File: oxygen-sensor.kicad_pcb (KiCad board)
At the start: 2 copper layers, 37.5 x 137.5 mm, 38 parts, among them J1 DEBUG, J2 UART, J3 I2C, U1 LM358, U2 LD1117S33TR_SOT223, U3 STM32F030K6Tx, Y1 Crystal

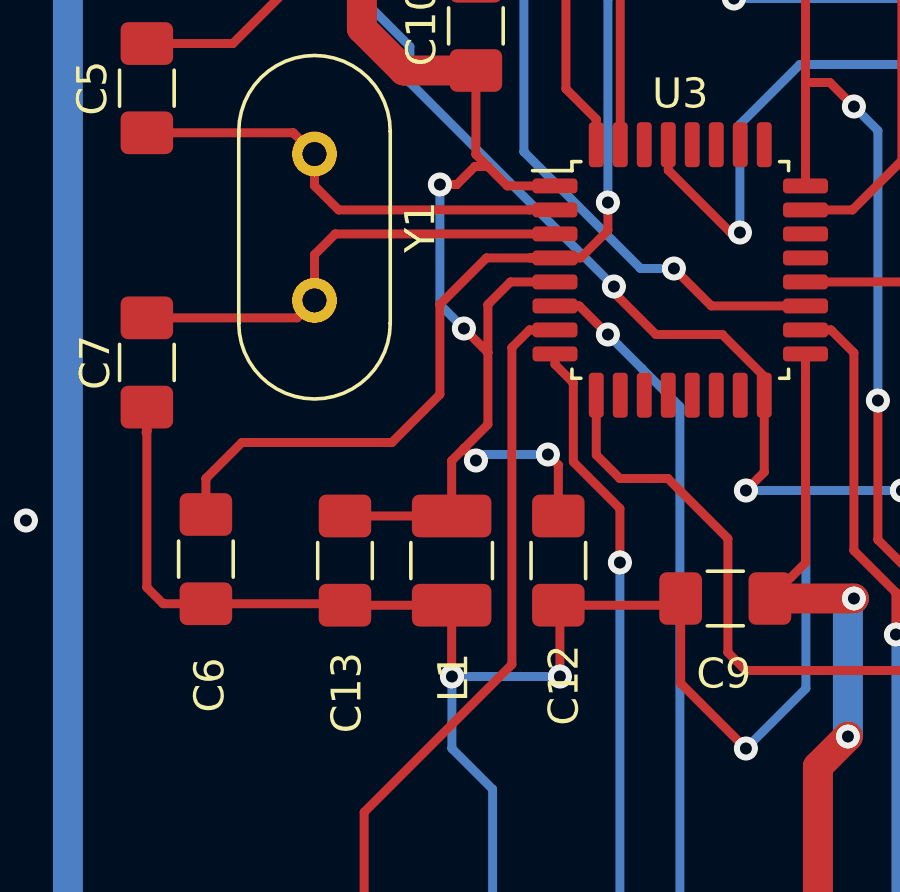
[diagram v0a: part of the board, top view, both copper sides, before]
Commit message: Fix short-circuit error
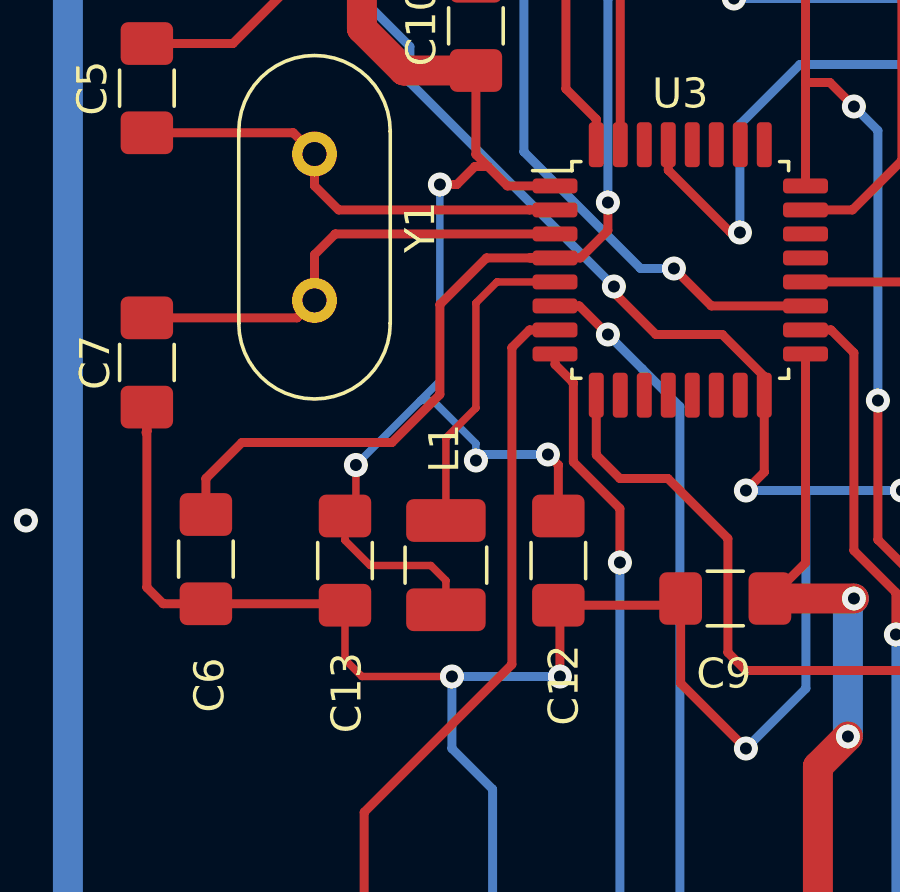
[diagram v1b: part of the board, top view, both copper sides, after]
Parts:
- moved L1 0.24 mm to (63.0, 74.5), turned to 270 degrees
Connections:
- L1 pad 1: GND -> Net-(L1-Pad1)
- U3 pad 5: +3V3 -> Net-(L1-Pad1)
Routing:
- net Net-(L1-Pad1): track 0.00 -> 10.6 mm
- net +3V3: track 302.4 -> 303.0 mm
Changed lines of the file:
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@@
     (thickness 1.6)
     (drawings 24)
-    (tracks 446)
+    (tracks 453)
     (zones 0)
     (modules 38)
-    (nets 37)
+    (nets 38)
   )
   (page A4)
@@
   (net 35 "Net-(U3-Pad28)")
   (net 36 "Net-(U3-Pad30)")
+  (net 37 "Net-(L1-Pad1)")
   (net_class Default "This is the default net class."
     (clearance 0.2)
@@
     (add_net "Net-(J3-Pad2)")
     (add_net "Net-(J3-Pad3)")
+    (add_net "Net-(L1-Pad1)")
     (add_net "Net-(R1-Pad1)")
     (add_net "Net-(R10-Pad1)")
@@
   )
   (module Inductor_SMD:L_1210_3225Metric_Pad1.42x2.65mm_HandSolder (layer F.Cu)
-    (at 63.192 74.3365 90)
+    (at 63 74.4875 270)
     (descr "Capacitor SMD 1210 (3225 Metric), square (rectangular) end terminal, IPC_7351 nominal with elongated pad for handsoldering. (Body size source: http://www.tortai-tech.com/upload/download/2011102023233369053.pdf), generated with kicad-footprint-generator")
     (tags "inductor handsolder")
     (attr smd)
-    (fp_text reference L1 (at -3.8955 0.054 90) (layer F.SilkS)
-      (effects (font (size 1 1) (thickness 0.15)))
-    )
-    (fp_text value 22uH (at 0 2.28 90) (layer F.Fab)
+    (fp_text reference L1 (at -3.8955 0.054 270) (layer F.SilkS)
+      (effects (font (size 1 1) (thickness 0.15)))
+    )
+    (fp_text value 22uH (at 0 2.28 270) (layer F.Fab)
       (effects (font (size 1 1) (thickness 0.15)))
     )
@@
     (fp_line (start 2.45 -1.58) (end 2.45 1.58) (layer F.CrtYd) (width 0.05))
     (fp_line (start 2.45 1.58) (end -2.45 1.58) (layer F.CrtYd) (width 0.05))
-    (fp_text user %R (at 0 0 90) (layer F.Fab)
+    (fp_text user %R (at 0 0 270) (layer F.Fab)
       (effects (font (size 0.8 0.8) (thickness 0.12)))
     )
-    (pad 1 smd roundrect (at -1.4875 0 90) (size 1.425 2.65) (layers F.Cu F.Paste F.Mask) (roundrect_rratio 0.175439)
-      (net 1 GND))
-    (pad 2 smd roundrect (at 1.4875 0 90) (size 1.425 2.65) (layers F.Cu F.Paste F.Mask) (roundrect_rratio 0.175439)
+    (pad 1 smd roundrect (at -1.4875 0 270) (size 1.425 2.65) (layers F.Cu F.Paste F.Mask) (roundrect_rratio 0.175439)
+      (net 37 "Net-(L1-Pad1)"))
+    (pad 2 smd roundrect (at 1.4875 0 270) (size 1.425 2.65) (layers F.Cu F.Paste F.Mask) (roundrect_rratio 0.175439)
       (net 8 +3V3))
     (model ${KISYS3DMOD}/Inductor_SMD.3dshapes/L_1210_3225Metric.wrl
@@
       (net 14 /NRST))
     (pad 5 smd roundrect (at -4.175 0.4) (size 1.5 0.5) (layers F.Cu F.Paste F.Mask) (roundrect_rratio 0.25)
-      (net 8 +3V3))
+      (net 37 "Net-(L1-Pad1)"))
     (pad 6 smd roundrect (at -4.175 1.2) (size 1.5 0.5) (layers F.Cu F.Paste F.Mask) (roundrect_rratio 0.25)
       (net 9 /OUT1))
@@
   (segment (start 59.587 75.775) (end 59.636 75.824) (width 0.3) (layer F.Cu) (net 1))
   (segment (start 55 75.775) (end 59.587 75.775) (width 0.3) (layer F.Cu) (net 1))
-  (segment (start 59.636 75.824) (end 63.192 75.824) (width 0.3) (layer F.Cu) (net 1))
   (segment (start 70.601 75.824) (end 70.825 75.6) (width 0.3) (layer F.Cu) (net 1))
   (segment (start 66.748 75.824) (end 70.601 75.824) (width 0.3) (layer F.Cu) (net 1))
-  (segment (start 63.192 75.824) (end 63.192 78.192) (width 0.3) (layer F.Cu) (net 1))
   (via (at 63.2 78.2) (size 0.8) (drill 0.4) (layers F.Cu B.Cu) (net 1))
   (segment (start 63.192 78.192) (end 63.2 78.2) (width 0.3) (layer F.Cu) (net 1))
@@
   (via (at 83 57) (size 0.8) (drill 0.4) (layers F.Cu B.Cu) (net 1))
   (via (at 63 86) (size 0.8) (drill 0.4) (layers F.Cu B.Cu) (net 1))
+  (segment (start 59.636 75.824) (end 59.636 77.636) (width 0.25) (layer F.Cu) (net 1))
+  (segment (start 60.2 78.2) (end 63.2 78.2) (width 0.25) (layer F.Cu) (net 1))
+  (segment (start 59.636 77.636) (end 60.2 78.2) (width 0.25) (layer F.Cu) (net 1))
   (segment (start 57.6 151.6) (end 62.4 151.6) (width 0.3) (layer F.Cu) (net 2))
   (segment (start 57.175 124.2) (end 57.2 124.225) (width 0.3) (layer F.Cu) (net 3))
@@
   (segment (start 78.375 135.425) (end 72.4 135.425) (width 0.3) (layer F.Cu) (net 7))
   (segment (start 81.4 132.4) (end 78.375 135.425) (width 0.3) (layer F.Cu) (net 7))
-  (segment (start 66.637 65.048) (end 65.152 65.048) (width 0.3) (layer F.Cu) (net 8))
-  (segment (start 65.152 65.048) (end 64.4 65.8) (width 0.3) (layer F.Cu) (net 8))
-  (segment (start 63.192 71.008) (end 63.192 72.849) (width 0.3) (layer F.Cu) (net 8))
   (segment (start 64 58) (end 64 60.8) (width 0.3) (layer F.Cu) (net 8))
   (segment (start 65.048 61.848) (end 66.637 61.848) (width 0.3) (layer F.Cu) (net 8))
@@
   (via (at 64 71) (size 0.8) (drill 0.4) (layers F.Cu B.Cu) (net 8))
   (segment (start 64.2 70.8) (end 64 71) (width 0.3) (layer B.Cu) (net 8))
-  (segment (start 64 71) (end 63.6 70.6) (width 0.3) (layer F.Cu) (net 8))
-  (segment (start 64.4 69.8) (end 63.6 70.6) (width 0.3) (layer F.Cu) (net 8))
-  (segment (start 63.6 70.6) (end 63.192 71.008) (width 0.3) (layer F.Cu) (net 8))
-  (segment (start 59.636 72.849) (end 63.192 72.849) (width 0.3) (layer F.Cu) (net 8))
   (segment (start 64.425 100.8) (end 64.425 112.225) (width 0.3) (layer F.Cu) (net 8))
   (segment (start 65.4 113.2) (end 67 113.2) (width 0.3) (layer F.Cu) (net 8))
@@
   (segment (start 63.765685 130.6) (end 63.2 130.6) (width 1) (layer B.Cu) (net 8))
   (segment (start 63.2 130.6) (end 58.6 130.6) (width 1) (layer B.Cu) (net 8))
-  (segment (start 64.4 67.4) (end 63.6 66.6) (width 0.3) (layer F.Cu) (net 8))
-  (via (at 63.6 66.6) (size 0.8) (drill 0.4) (layers F.Cu B.Cu) (net 8))
-  (segment (start 64.4 67.4) (end 64.4 69.8) (width 0.3) (layer F.Cu) (net 8))
-  (segment (start 64.4 65.8) (end 64.4 67.4) (width 0.3) (layer F.Cu) (net 8))
   (via (at 62.8 61.8) (size 0.8) (drill 0.4) (layers F.Cu B.Cu) (net 8))
-  (segment (start 63.6 66.6) (end 62.8 65.8) (width 0.3) (layer B.Cu) (net 8))
-  (segment (start 62.8 65.8) (end 62.8 61.8) (width 0.3) (layer B.Cu) (net 8))
   (segment (start 63.965685 61.2) (end 64.4 61.2) (width 0.3) (layer F.Cu) (net 8))
   (segment (start 62.8 61.8) (end 63.365685 61.8) (width 0.3) (layer F.Cu) (net 8))
@@
   (segment (start 64 60.8) (end 64.4 61.2) (width 0.3) (layer F.Cu) (net 8))
   (segment (start 64.4 61.2) (end 65.048 61.848) (width 0.3) (layer F.Cu) (net 8))
+  (via (at 60 71.15) (size 0.8) (drill 0.4) (layers F.Cu B.Cu) (net 8))
+  (segment (start 62.8 61.8) (end 62.8 68.35) (width 0.25) (layer B.Cu) (net 8))
+  (segment (start 60 72.485) (end 59.636 72.849) (width 0.25) (layer F.Cu) (net 8))
+  (segment (start 60 71.15) (end 60 72.485) (width 0.25) (layer F.Cu) (net 8))
+  (segment (start 59.636 73.6615) (end 60.4745 74.5) (width 0.25) (layer F.Cu) (net 8))
+  (segment (start 59.636 72.849) (end 59.636 73.6615) (width 0.25) (layer F.Cu) (net 8))
+  (segment (start 60.4745 74.5) (end 62.5 74.5) (width 0.25) (layer F.Cu) (net 8))
+  (segment (start 63 75) (end 63 75.975) (width 0.25) (layer F.Cu) (net 8))
+  (segment (start 62.5 74.5) (end 63 75) (width 0.25) (layer F.Cu) (net 8))
+  (segment (start 64 70.434315) (end 62.565685 69) (width 0.25) (layer B.Cu) (net 8))
+  (segment (start 64 71) (end 64 70.434315) (width 0.25) (layer B.Cu) (net 8))
+  (segment (start 62.565685 69) (end 62.15 69) (width 0.25) (layer B.Cu) (net 8))
+  (segment (start 62.15 69) (end 60 71.15) (width 0.25) (layer B.Cu) (net 8))
+  (segment (start 62.8 68.35) (end 62.15 69) (width 0.25) (layer B.Cu) (net 8))
   (segment (start 52.6 138.8) (end 56.4 138.8) (width 0.3) (layer F.Cu) (net 9))
   (segment (start 57.075 139.475) (end 63.495 139.475) (width 0.3) (layer F.Cu) (net 9))
@@
   (segment (start 68.812 54.52) (end 68.78 54.488) (width 0.3) (layer F.Cu) (net 23))
   (segment (start 68.812 60.473) (end 68.812 54.52) (width 0.3) (layer F.Cu) (net 23))
+  (segment (start 63 73) (end 63 70.25) (width 0.25) (layer F.Cu) (net 37))
+  (segment (start 63 70.25) (end 64 69.25) (width 0.25) (layer F.Cu) (net 37))
+  (segment (start 64 69.25) (end 64 65.75) (width 0.25) (layer F.Cu) (net 37))
+  (segment (start 64.702 65.048) (end 66.637 65.048) (width 0.25) (layer F.Cu) (net 37))
+  (segment (start 64 65.75) (end 64.702 65.048) (width 0.25) (layer F.Cu) (net 37))
   (zone (net 1) (net_name GND) (layer F.Cu) (hatch edge 0.508)
     (connect_pads (clearance 0.508))
